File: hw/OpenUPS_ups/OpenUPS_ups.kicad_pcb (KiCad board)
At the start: 4 copper layers, 90 x 62 mm, 286 parts, among them J1001 USB4105-GF-A, J101 Barrel Jack, J102 XT30PW-M, J103 XT30PW-M, J104 S2B-PH-K_1x02, J105 S2B-PH-K_1x02, J106 Screw Terminal, J107 Screw Terminal, J108 Screw Terminal, J109 JST XH, J110 JST XH, J501 Conn_01x03, J701 0022053031, J702 0022053031, J901 Qwiic, J902 Qwiic, Q1001 2N7002, Q301 AON7534, Q302 AON7534, Q303 AON7534, Q304 AON7534, Q401 2N7002, Q402 AON7534, Q403 AON7534, Q404 AON7534, Q405 AON7534, Q601 AON7534, Q602 AON7534, Q603 AON7534, Q604 AON7534, Q701 2N7002, Q702 2N7002, U1001 MCP6547, U1002 AP22814BW5, U1003 NUP2301MW6T1G, U101 AVR32DB48x-xPT, U102 NUP2301MW6T1G, U201 TPS51397A, U202 INA180A3, U301 NCP81599, U401 NCP431, U402 BD99950, U403 MCP6001R, U404 DZDH0401DW, U405 INA180A1, U601 NCP81599, U701 NUP2301MW6T1G, U702 NUP2301MW6T1G, U801 AP7383-33W5, U901 π220N31

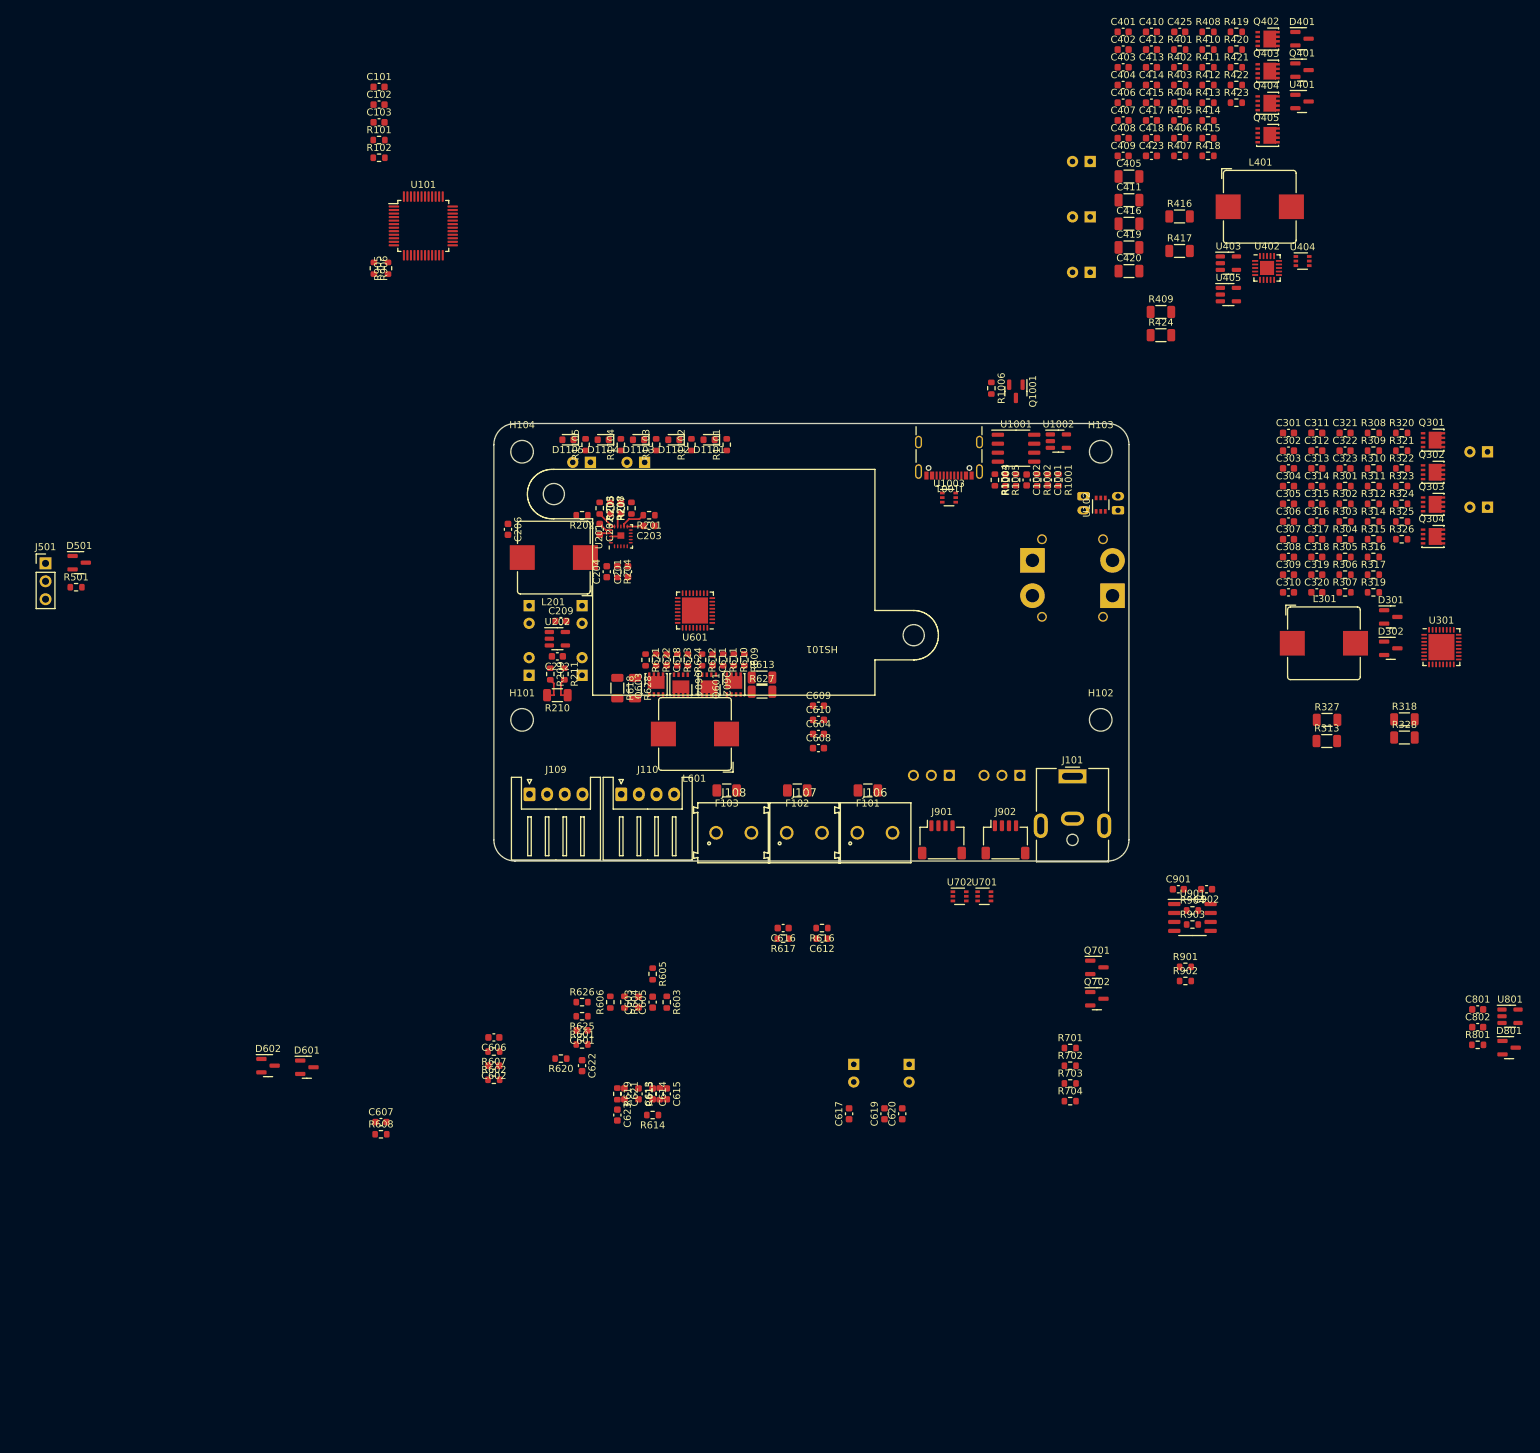
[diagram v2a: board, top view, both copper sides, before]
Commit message: Issue #23: Thin BAT54 diodes in converters
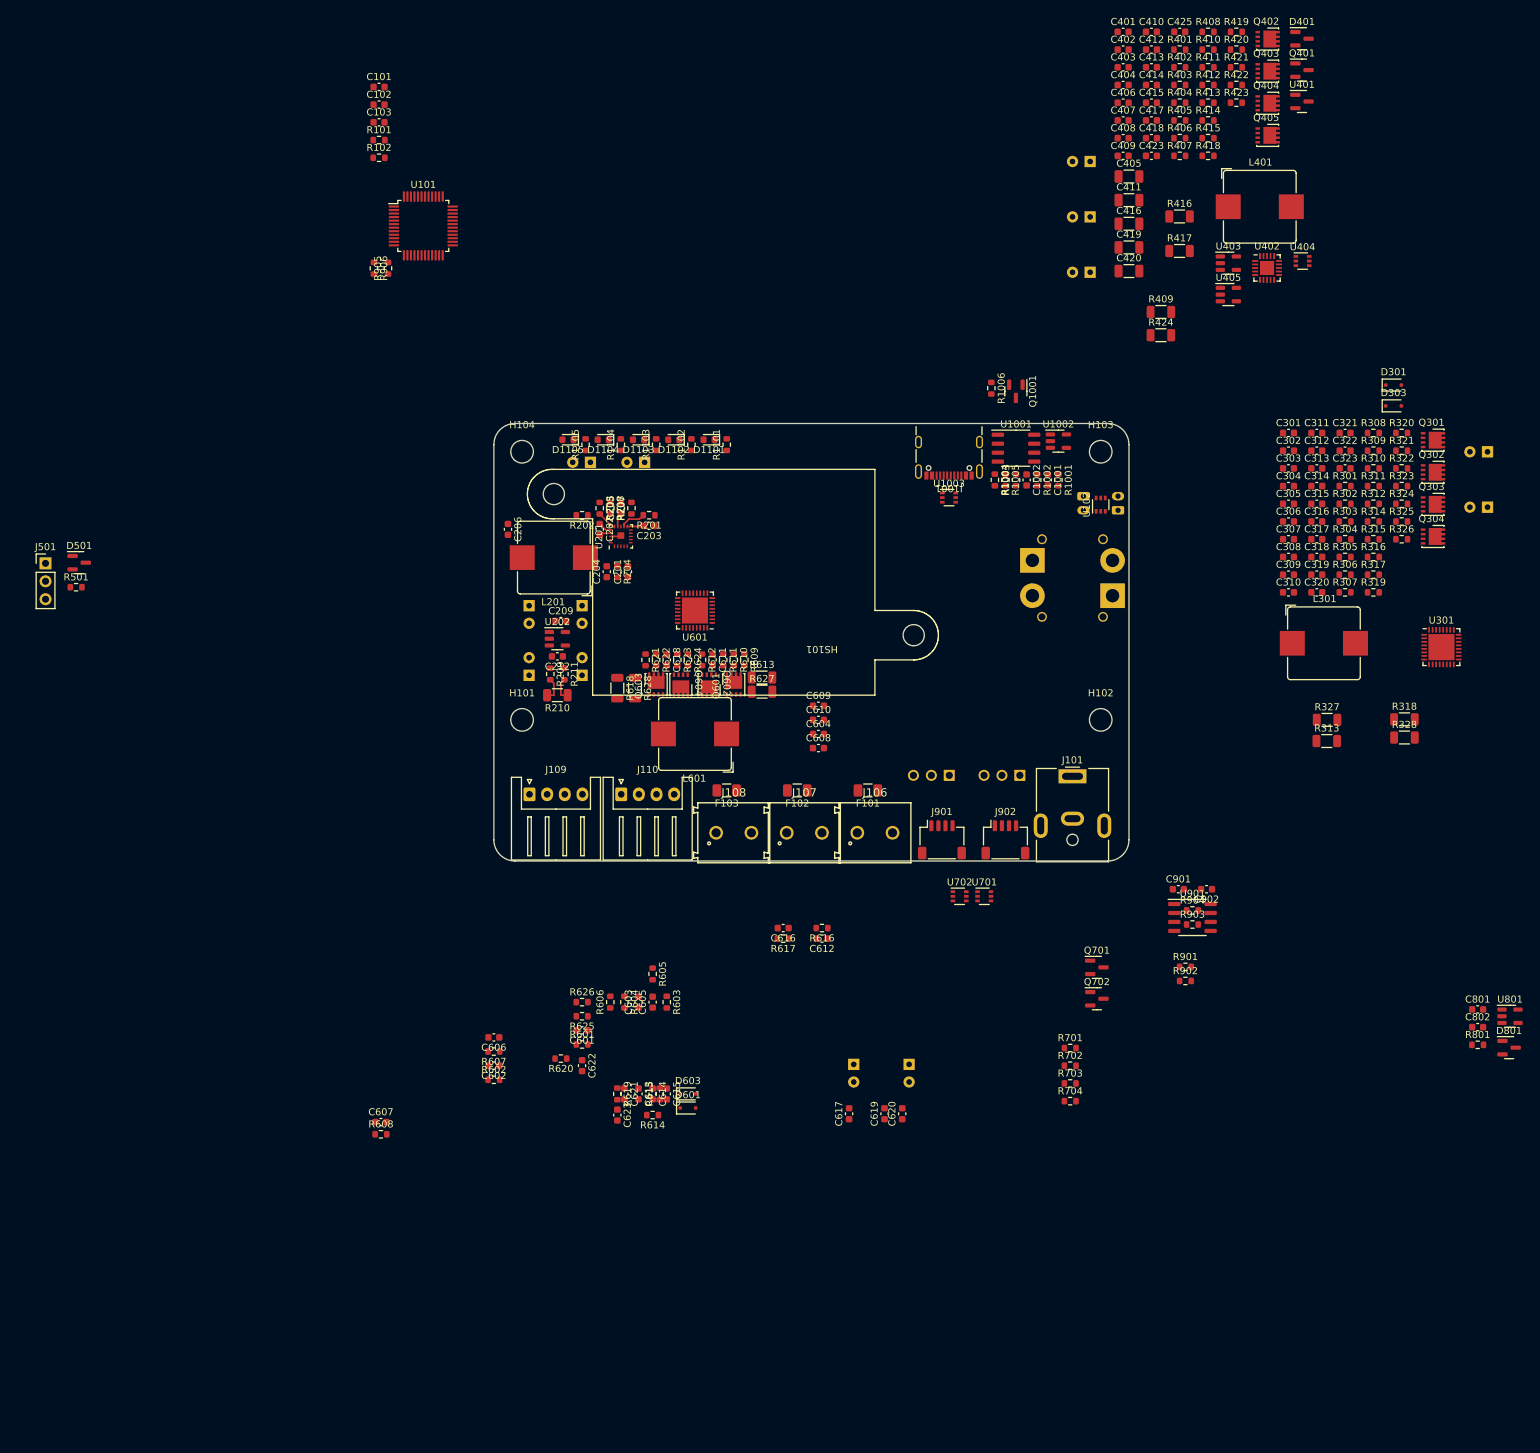
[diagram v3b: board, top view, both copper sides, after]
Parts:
- removed D302, D602: BAT54C, Package_TO_SOT_SMD:SOT-23
- added D303: BAT54J, Diode_SMD:D_SOD-323F, F.Cu at (210.5, 69.5)
- added D603: BAT54J, Diode_SMD:D_SOD-323F, F.Cu at (110.5, 167.0)
- D301, D601: value BAT54C -> BAT54J; footprint Package_TO_SOT_SMD:SOT-23 -> Diode_SMD:D_SOD-323F
- moved D601 54.3 mm to (110.5, 169.0)
- moved D301 32.9 mm to (210.5, 66.5)
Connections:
- D301 pad 1: /Adj_Buck_Boost/VDRV -> Net-(D301-K)
- D601 pad 1: /12V Buck_Boost/VDRV -> Net-(D601-K)
- R311 pad 1: Net-(U301B-BST1) -> Net-(D303-K)
- R323 pad 1: Net-(U301C-BST2) -> Net-(D301-K)
- R611 pad 1: Net-(U601B-BST1) -> Net-(D603-K)
- R623 pad 1: Net-(U601C-BST2) -> Net-(D601-K)
- U301 pad 25: Net-(U301C-BST2) -> Net-(D301-K)
- U301 pad 32: Net-(U301B-BST1) -> Net-(D303-K)
- U601 pad 25: Net-(U601C-BST2) -> Net-(D601-K)
- U601 pad 32: Net-(U601B-BST1) -> Net-(D603-K)

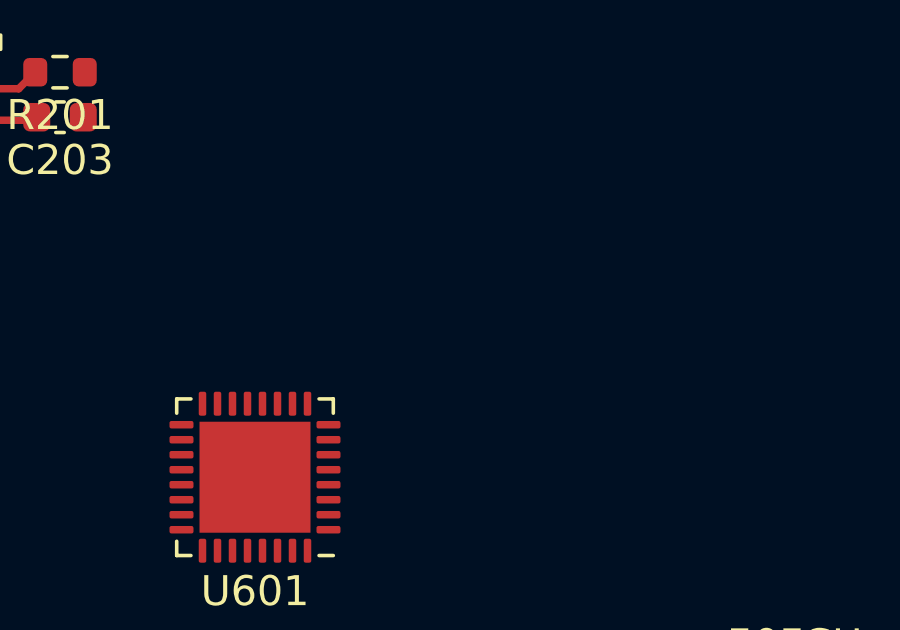
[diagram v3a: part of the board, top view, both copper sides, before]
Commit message: Issue #23: Added thermal sensor
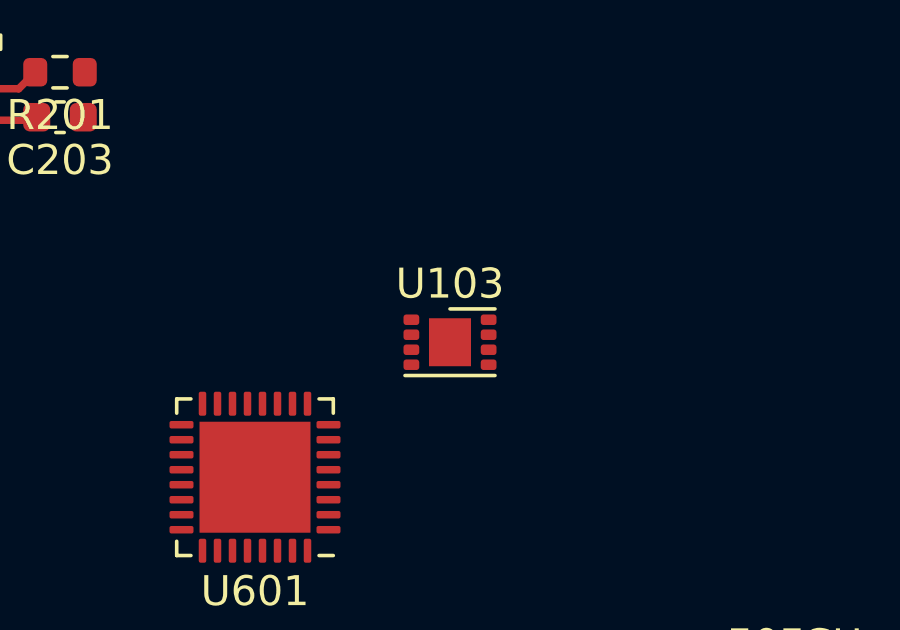
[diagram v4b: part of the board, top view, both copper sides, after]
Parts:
- added U103: LM75BTP,147, Package_SON:SON-8-1EP_3x2mm_P0.5mm_EP1.4x1.6mm, F.Cu at (118.0, 94.0)
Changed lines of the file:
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@@
   (net 211 "Net-(D601-K)")
   (net 212 "Net-(D603-K)")
+  (net 213 "/T_OS")
   (footprint "Resistor_SMD:R_0603_1608Metric" (layer "F.Cu")
     (at 211.65 88.4)
@@
       (offset (xyz 0 0 0))
       (scale (xyz 1 1 1))
+      (rotate (xyz 0 0 0))
+    )
+  )
+  (footprint "Package_SON:SON-8-1EP_3x2mm_P0.5mm_EP1.4x1.6mm" (layer "F.Cu")
+    (at 118 94)
+    (descr "SON, 8 Pin (http://www.fujitsu.com/downloads/MICRO/fsa/pdf/products/memory/fram/MB85RS16-DS501-00014-6v0-E.pdf), generated with kicad-footprint-generator ipc_noLead_generator.py")
+    (tags "SON NoLead")
+    (property "Sheetfile" "OpenUPS_ups.kicad_sch")
+    (property "Sheetname" "")
+    (property "ki_description" "Digital Temperature Sensor & Thermal Watchdog with LP on I2C and bus fault timeout, SOIC-8 and VSSOP-8")
+    (property "ki_keywords" "Temperature sensor")
+    (attr smd)
+    (fp_text reference "U103" (at 0 -1.95) (layer "F.SilkS")
+        (effects (font (size 1 1) (thickness 0.15)))
+    )
+    (fp_text value "LM75BTP,147" (at 0 1.95) (layer "F.Fab")
+        (effects (font (size 1 1) (thickness 0.15)))
+    )
+    (fp_text user "${REFERENCE}" (at 0 0) (layer "F.Fab")
+        (effects (font (size 0.75 0.75) (thickness 0.11)))
+    )
+    (fp_line (start -1.5 1.11) (end 1.5 1.11)
+      (stroke (width 0.12) (type solid)) (layer "F.SilkS"))
+    (fp_line (start 0 -1.11) (end 1.5 -1.11)
+      (stroke (width 0.12) (type solid)) (layer "F.SilkS"))
+    (fp_line (start -1.8 -1.25) (end -1.8 1.25)
+      (stroke (width 0.05) (type solid)) (layer "F.CrtYd"))
+    (fp_line (start -1.8 1.25) (end 1.8 1.25)
+      (stroke (width 0.05) (type solid)) (layer "F.CrtYd"))
+    (fp_line (start 1.8 -1.25) (end -1.8 -1.25)
+      (stroke (width 0.05) (type solid)) (layer "F.CrtYd"))
+    (fp_line (start 1.8 1.25) (end 1.8 -1.25)
+      (stroke (width 0.05) (type solid)) (layer "F.CrtYd"))
+    (fp_line (start -1.5 -0.5) (end -1 -1)
+      (stroke (width 0.1) (type solid)) (layer "F.Fab"))
+    (fp_line (start -1.5 1) (end -1.5 -0.5)
+      (stroke (width 0.1) (type solid)) (layer "F.Fab"))
+    (fp_line (start -1 -1) (end 1.5 -1)
+      (stroke (width 0.1) (type solid)) (layer "F.Fab"))
+    (fp_line (start 1.5 -1) (end 1.5 1)
+      (stroke (width 0.1) (type solid)) (layer "F.Fab"))
+    (fp_line (start 1.5 1) (end -1.5 1)
+      (stroke (width 0.1) (type solid)) (layer "F.Fab"))
+    (pad "" smd roundrect (at -0.35 -0.4) (size 0.56 0.64) (layers "F.Paste") (roundrect_rratio 0.25))
+    (pad "" smd roundrect (at -0.35 0.4) (size 0.56 0.64) (layers "F.Paste") (roundrect_rratio 0.25))
+    (pad "" smd roundrect (at 0.35 -0.4) (size 0.56 0.64) (layers "F.Paste") (roundrect_rratio 0.25))
+    (pad "" smd roundrect (at 0.35 0.4) (size 0.56 0.64) (layers "F.Paste") (roundrect_rratio 0.25))
+    (pad "1" smd roundrect (at -1.2875 -0.75) (size 0.525 0.35) (layers "F.Cu" "F.Paste" "F.Mask") (roundrect_rratio 0.25)
+      (net 128 "/I2C_I_SDA") (pinfunction "SDA") (pintype "bidirectional"))
+    (pad "2" smd roundrect (at -1.2875 -0.25) (size 0.525 0.35) (layers "F.Cu" "F.Paste" "F.Mask") (roundrect_rratio 0.25)
+      (net 129 "/I2C_I_SCL") (pinfunction "SCL") (pintype "input"))
+    (pad "3" smd roundrect (at -1.2875 0.25) (size 0.525 0.35) (layers "F.Cu" "F.Paste" "F.Mask") (roundrect_rratio 0.25)
+      (net 213 "/T_OS") (pinfunction "O.S.") (pintype "open_collector"))
+    (pad "4" smd roundrect (at -1.2875 0.75) (size 0.525 0.35) (layers "F.Cu" "F.Paste" "F.Mask") (roundrect_rratio 0.25)
+      (net 2 "GND") (pinfunction "GND") (pintype "power_in"))
+    (pad "5" smd roundrect (at 1.2875 0.75) (size 0.525 0.35) (layers "F.Cu" "F.Paste" "F.Mask") (roundrect_rratio 0.25)
+      (net 2 "GND") (pinfunction "A2") (pintype "input"))
+    (pad "6" smd roundrect (at 1.2875 0.25) (size 0.525 0.35) (layers "F.Cu" "F.Paste" "F.Mask") (roundrect_rratio 0.25)
+      (net 2 "GND") (pinfunction "A1") (pintype "input"))
+    (pad "7" smd roundrect (at 1.2875 -0.25) (size 0.525 0.35) (layers "F.Cu" "F.Paste" "F.Mask") (roundrect_rratio 0.25)
+      (net 2 "GND") (pinfunction "A0") (pintype "input"))
+    (pad "8" smd roundrect (at 1.2875 -0.75) (size 0.525 0.35) (layers "F.Cu" "F.Paste" "F.Mask") (roundrect_rratio 0.25)
+      (net 1 "+3.3VA") (pinfunction "+Vs") (pintype "power_in"))
+    (pad "9" smd rect (at 0 0) (size 1.4 1.6) (layers "F.Cu" "F.Mask"))
+    (model "${KICAD6_3DMODEL_DIR}/Package_SON.3dshapes/SON-8-1EP_3x2mm_P0.5mm_EP1.4x1.6mm.wrl"
+      (offset (xyz 0 0 0))
+      (scale (xyz 1 1 1))

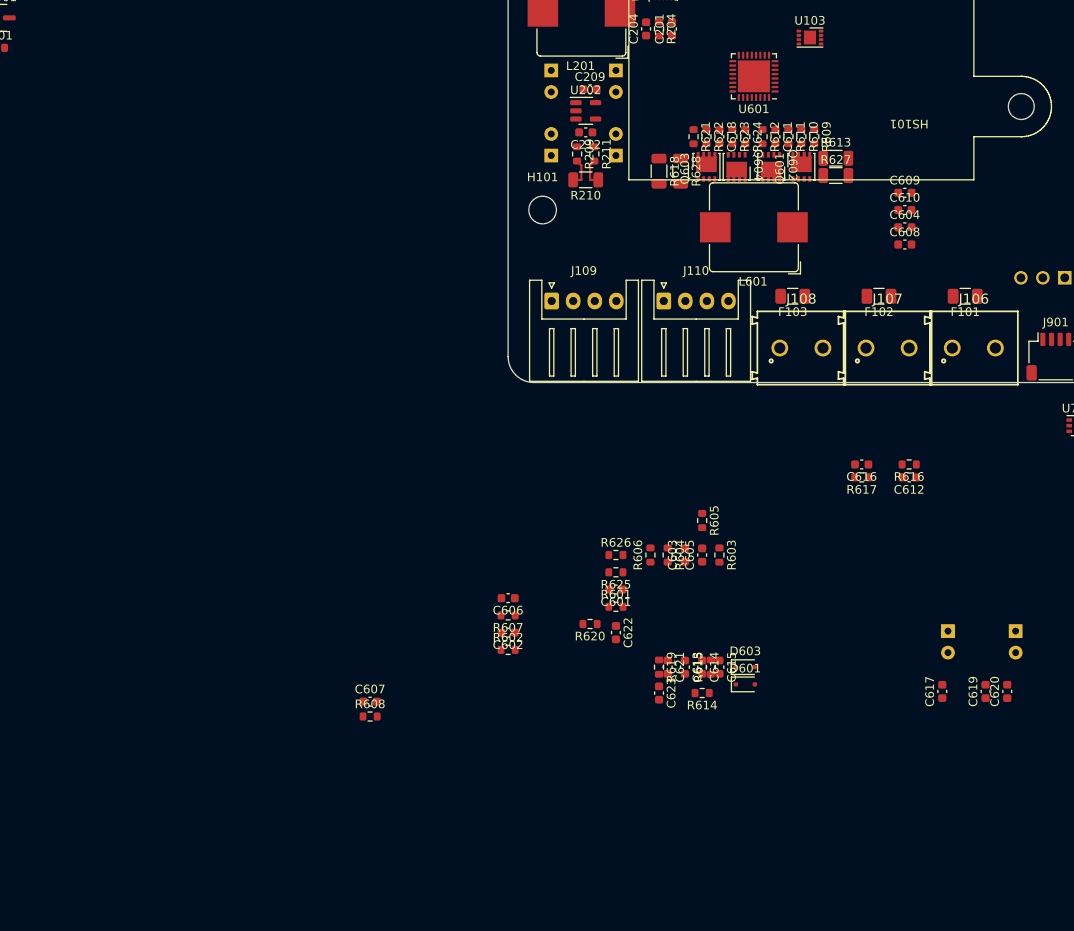
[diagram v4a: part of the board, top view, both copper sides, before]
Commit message: 12V converter layout
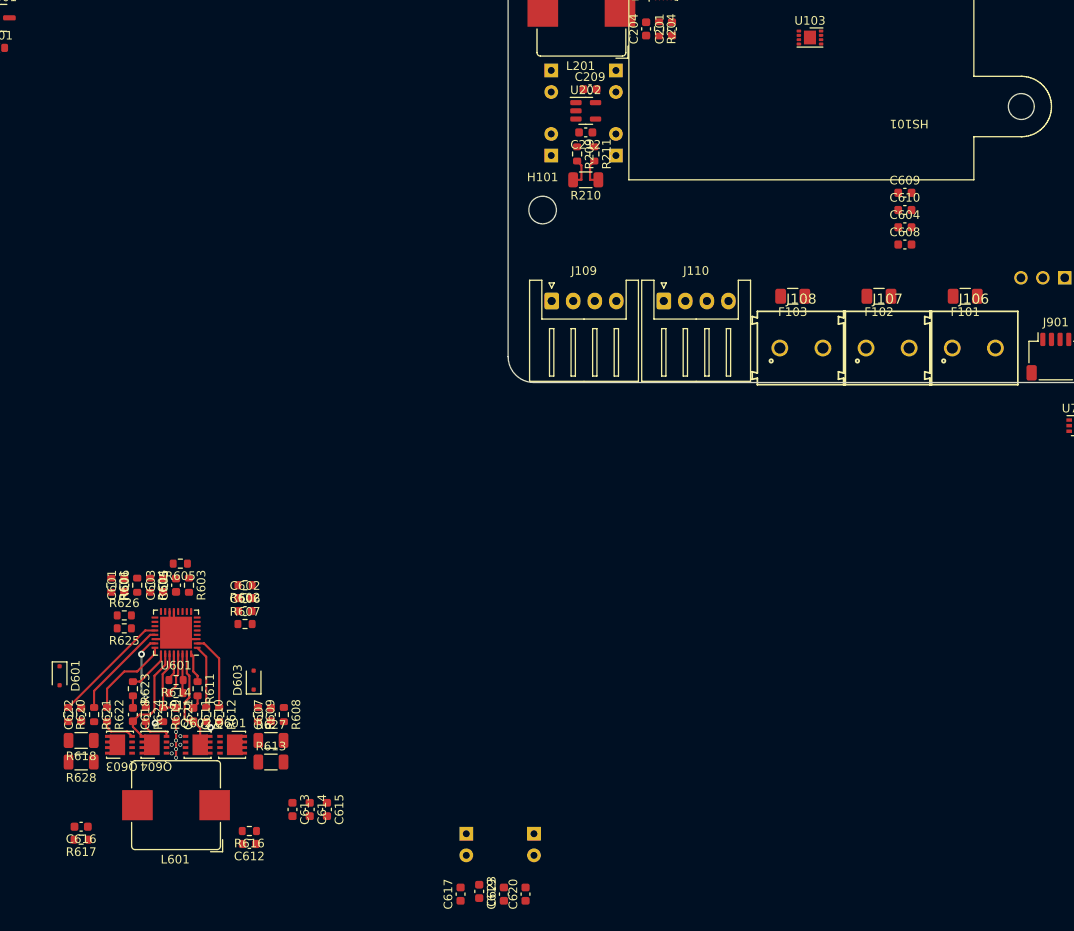
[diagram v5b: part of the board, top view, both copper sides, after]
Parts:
- moved C616 99.8 mm to (33.5, 185.5)
- moved R617 99.8 mm to (33.5, 187.0)
- moved R628 97.6 mm to (33.5, 178.0), turned to 180 degrees
- moved R621 96.5 mm to (35.0, 172.5)
- moved R622 96.5 mm to (36.5, 172.5)
- moved R624 96.5 mm to (41.0, 172.5)
- moved R610 96.2 mm to (48.0, 172.5)
- moved R613 95.9 mm to (55.5, 178.0)
- moved C618 95.5 mm to (39.5, 172.5)
- moved Q603 95.5 mm to (38.0, 176.0), turned to 180 degrees
- moved C611 95.1 mm to (46.5, 172.5)
- moved Q604 95.1 mm to (42.0, 176.0), turned to 180 degrees
- moved L601 94.8 mm to (44.5, 183.0)
- moved R623 94.5 mm to (39.5, 169.5)
- moved Q602 94.4 mm to (47.0, 176.0), turned to 0 degrees
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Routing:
- net GND: track 3.34 -> 18.4 mm, vias 0 -> 4
- net Net-(U601C-CSN2): track 0.00 -> 13.7 mm
- net Net-(U601C-VSW2): track 0.00 -> 12.3 mm
- net Net-(U601B-VSW1): track 0.00 -> 12.1 mm
- net Net-(U601C-CSP2): track 0.00 -> 11.7 mm
- net Net-(U601C-HSG2): track 0.00 -> 10.1 mm
- net Net-(U601B-LSG1): track 0.00 -> 8.95 mm
- net Net-(U601C-LSG2): track 0.00 -> 8.60 mm, vias 0 -> 6
- net Net-(U601C-V2): track 0.00 -> 8.10 mm
- net Net-(U601B-HSG1): track 0.00 -> 7.36 mm
- net Net-(D601-K): track 0.00 -> 5.05 mm
- net /12V Buck_Boost/VDRV: track 0.00 -> 5.00 mm
- net Net-(U601A-VCC): track 0.00 -> 4.58 mm
- net Net-(Q603-G): track 0.00 -> 4.00 mm
- net Net-(Q604-G): track 0.00 -> 3.73 mm
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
